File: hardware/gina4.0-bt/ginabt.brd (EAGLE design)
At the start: 15.7 x 13.3 mm, 27 parts, among them U1 CC2541, U2 MPU-9150, U3 CCDEBUGGER, U5 TPS71530

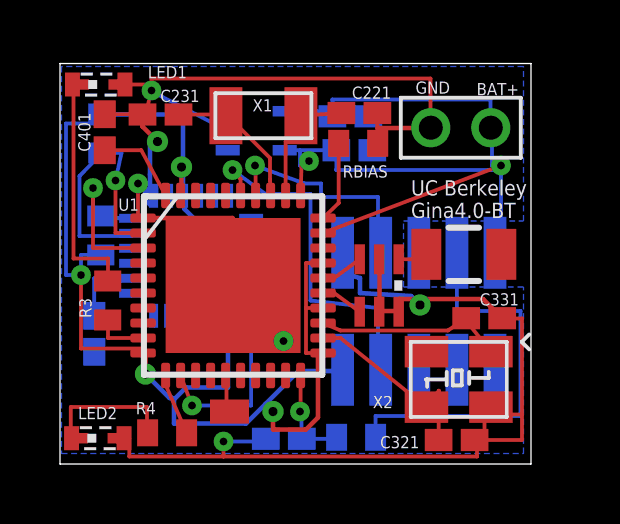
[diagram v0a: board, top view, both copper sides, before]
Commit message: fixed bad trace on BOT plane gerbers no longer valid!!!
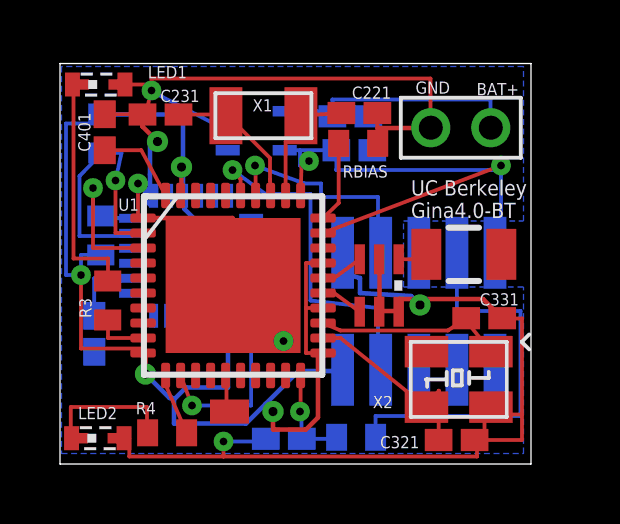
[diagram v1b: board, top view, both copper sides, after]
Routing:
- net +3V3: track 67.9 -> 66.4 mm
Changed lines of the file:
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@@
 <?xml version="1.0" encoding="utf-8"?>
 <!DOCTYPE eagle SYSTEM "eagle.dtd">
-<eagle version="6.2">
+<eagle version="6.5.0">
 <drawing>
 <settings>
@@
 </class>
 </classes>
-<designrules>
+<designrules name="default">
 <description language="de">&lt;b&gt;EAGLE Design Rules&lt;/b&gt;
 &lt;p&gt;
@@
 <wire x1="9.07" y1="7.05" x2="8.5" y2="7.05" width="0.127" layer="1"/>
 <wire x1="8.5" y1="7.05" x2="8.5" y2="5.55" width="0.127" layer="1"/>
-<wire x1="15" y1="10.3" x2="14.7" y2="10.3" width="0.127" layer="16"/>
-<wire x1="14.7" y1="10.3" x2="14.7" y2="11.5" width="0.127" layer="16"/>
 <wire x1="1.69" y1="11.7" x2="0.5" y2="11.7" width="0.127" layer="16"/>
 <wire x1="0.5" y1="11.7" x2="0.5" y2="6.65" width="0.127" layer="16"/>
